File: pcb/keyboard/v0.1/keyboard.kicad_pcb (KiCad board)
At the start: 2 copper layers, 80.8 x 79.7 mm, 142 parts, among them J1 USB2.0, J2 SWD, SW1 BACKTICK, SW10 9, SW11 0, SW12 BACKSPACE, SW13 TAB, SW14 Q, SW15 W, SW16 E, SW17 R, SW18 T, SW19 Y, SW2 1, SW20 U, SW21 I, SW22 O, SW23 P, SW24 RETURN, SW25 CAPS, SW26 A, SW27 S, SW28 D, SW29 F, SW3 2, SW30 G, SW31 H, SW32 J, SW33 K, SW34 L, SW35 SEMI, SW36 QUOTE, SW37 LSHIFT, SW38 Z, SW39 X, SW4 3, SW40 C, SW41 V, SW42 B, SW43 N, SW44 M, SW45 COMMA, SW46 DOT, SW47 QUEST, SW48 RSHIFT, SW49 FN, SW5 4, SW50 LCTRL, SW51 LSUPER, SW52 LALT, SW53 SPACE, SW54 RALT, SW55 RSUPER, SW56 MENU, SW57 RCTRL, SW58 C1, SW59 C2, SW6 5, SW60 C3, SW61 C4, SW62 C5, SW63 C6, SW7 6, SW8 7, SW9 8, U1 MDBT50Q-P1MV2, Y1 32.768

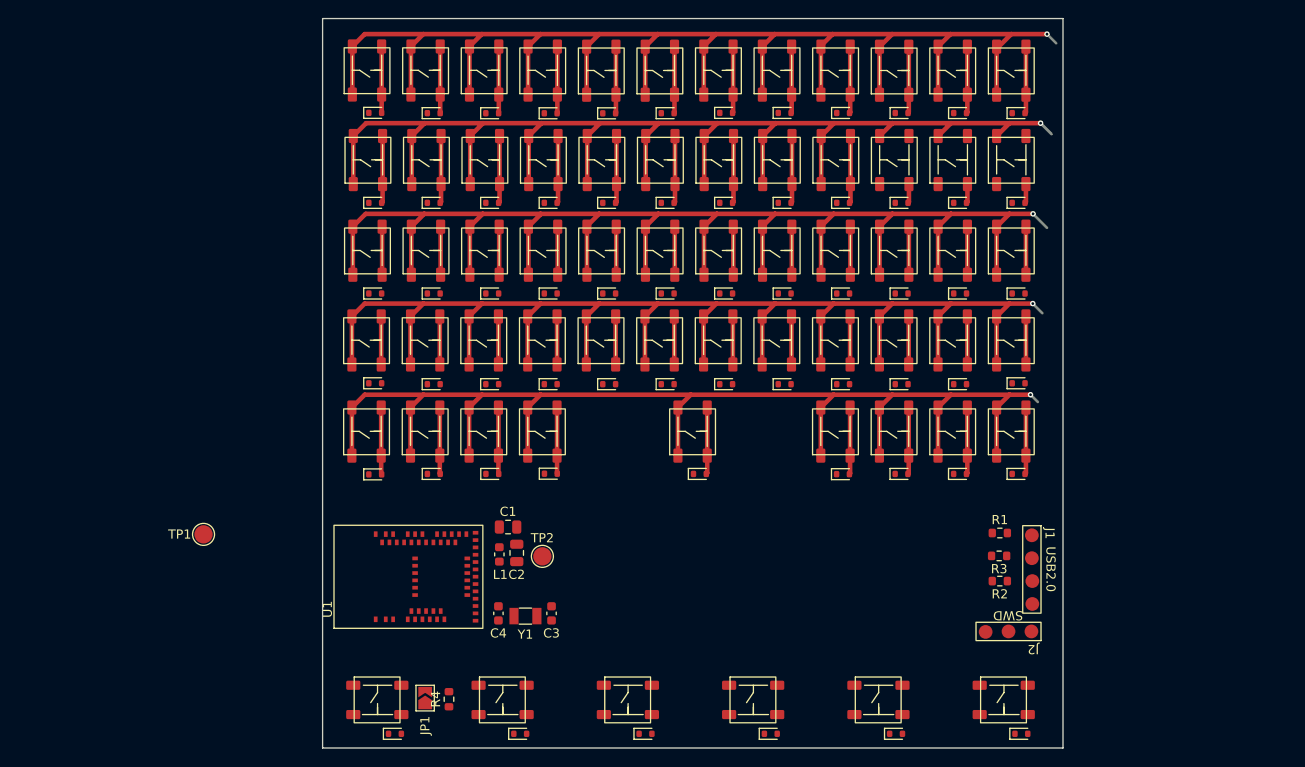
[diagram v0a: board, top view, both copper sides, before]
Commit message: Add RF keepout zone for main chip
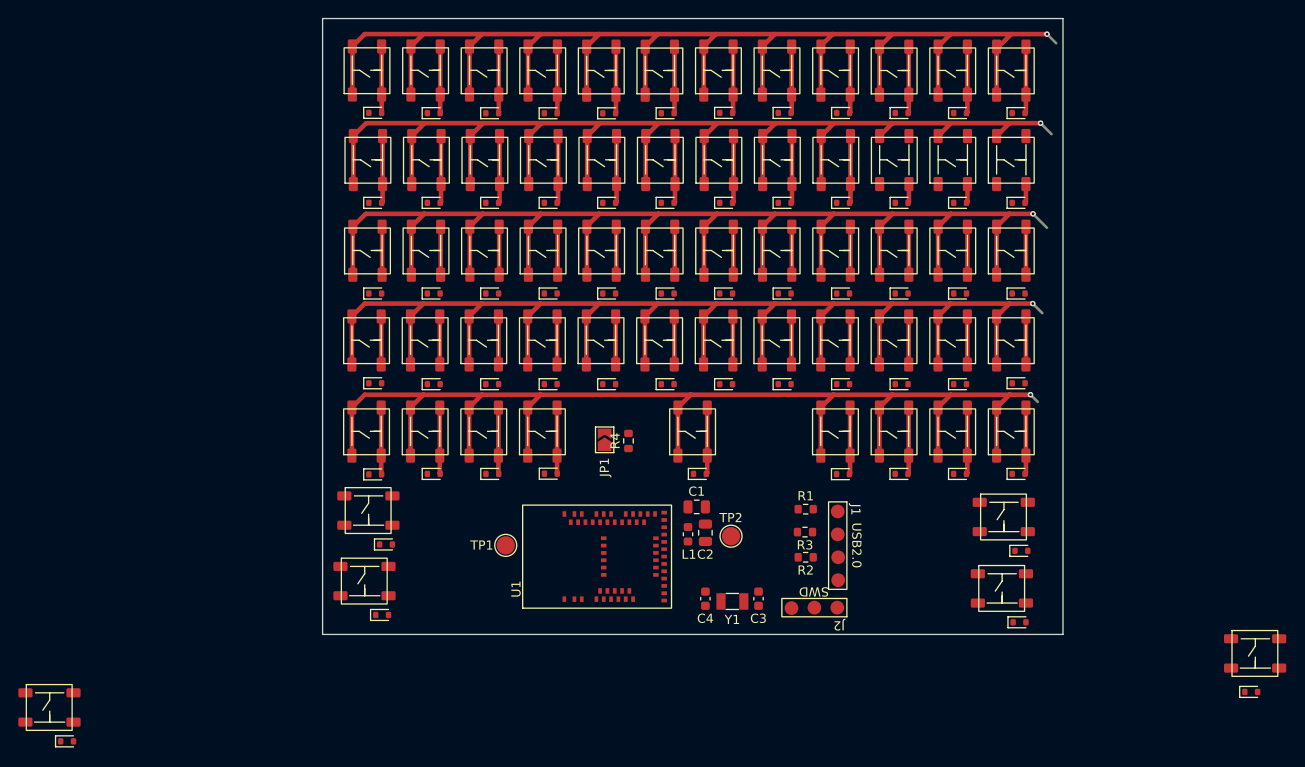
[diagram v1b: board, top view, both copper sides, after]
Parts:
- moved D60 63.2 mm to (28.5, 112.2)
- moved SW60 63.2 mm to (23.9, 106.9)
- moved JP1 34.3 mm to (87.2, 79.3)
- moved R4 34.3 mm to (89.8, 79.4)
- moved SW61 33.9 mm to (128.2, 86.1)
- moved D61 33.9 mm to (132.7, 91.4)
- moved TP1 33.0 mm to (76.4, 90.8)
- moved SW63 27.9 mm to (155.6, 101.0)
- moved D63 25.5 mm to (157.8, 106.8)
- moved Y1 22.7 mm to (101.2, 96.9)
- moved C4 22.7 mm to (98.2, 96.6)
- moved C3 22.7 mm to (104.0, 96.6)
- moved J2 21.4 mm to (112.6, 97.6)
- moved R3 21.4 mm to (109.1, 89.3)
- moved J1 21.4 mm to (112.7, 87.1)
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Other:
- board size 80.8 x 79.7 mm -> 80.8 x 67.2 mm
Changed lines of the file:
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@@
 	(footprint "TH-A1OC:tact_switch_4.5x4.5_PTS647"
 		(layer "F.Cu")
-		(at 73.43 106.075)
+		(at 58.35 93.1)
 		(property "Reference" "SW59"
 			(at 1 5 0)
@@
 	(footprint "TH-A1OC:tact_switch_4.5x4.5_PTS647"
 		(layer "F.Cu")
-		(at 59.75 106.075)
+		(at 58.775 85.4)
 		(property "Reference" "SW58"
 			(at 1 5 0)
@@
 	(footprint "Resistor_SMD:R_0603_1608Metric"
 		(layer "F.Cu")
-		(at 130.275 91.95 180)
+		(at 109.075 89.35 180)
 		(descr "Resistor SMD 0603 (1608 Metric), square (rectangular) end terminal, IPC-7351 nominal, (Body size source: IPC-SM-782 page 72, https://www.pcb-3d.com/wordpress/wp-content/uploads/ipc-sm-782a_amendment_1_and_2.pdf), generated with kicad-footprint-generator")
 		(tags "resistor")
@@
 	(footprint "TH-A1OC:th_pogo_pins_4"
 		(layer "F.Cu")
-		(at 133.85 89.7 -90)
+		(at 112.65 87.1 -90)
 		(property "Reference" "J1"
 			(at -0.2 -1.95 270)
@@
 	(footprint "Diode_SMD:D_SOD-523"
 		(layer "F.Cu")
-		(at 77.98 111.375)
+		(at 62.9 98.4)
 		(descr "http://www.diodes.com/datasheets/ap02001.pdf p.144")
 		(tags "Diode SOD523")
@@
 	(footprint "Capacitor_SMD:C_0805_2012Metric"
 		(layer "F.Cu")
-		(at 77.6 91.625 90)
+		(at 98.2 89.425 90)
 		(descr "Capacitor SMD 0805 (2012 Metric), square (rectangular) end terminal, IPC-7351 nominal, (Body size source: IPC-SM-782 page 76, https://www.pcb-3d.com/wordpress/wp-content/uploads/ipc-sm-782a_amendment_1_and_2.pdf, https://docs.google.com/spreadsheets/d/1BsfQQcO9C6DZCsRaXUlFlo91Tg2WpOkGARC1WS5S8t0/edit?usp=sharing), generated with kicad-footprint-generator")
 		(tags "capacitor")
@@
 	(footprint "TestPoint:TestPoint_Pad_D2.0mm"
 		(layer "F.Cu")
-		(at 43.4 89.6)
+		(at 76.4 90.8)
 		(descr "SMD pad as test Point, diameter 2.0mm")
 		(tags "test point SMD pad")
@@
 	(footprint "TH-A1OC:tact_switch_4.5x4.5_PTS647"
 		(layer "F.Cu")
-		(at 100.79 106.075)
+		(at 128.15 86.1)
 		(property "Reference" "SW61"
 			(at 1 5 0)
@@
 	(footprint "Capacitor_SMD:C_0603_1608Metric"
 		(layer "F.Cu")
-		(at 75.6 98.225 90)
+		(at 98.2 96.625 90)
 		(descr "Capacitor SMD 0603 (1608 Metric), square (rectangular) end terminal, IPC-7351 nominal, (Body size source: IPC-SM-782 page 76, https://www.pcb-3d.com/wordpress/wp-content/uploads/ipc-sm-782a_amendment_1_and_2.pdf), generated with kicad-footprint-generator")
 		(tags "capacitor")
@@
 	(footprint "Diode_SMD:D_SOD-523"
 		(layer "F.Cu")
-		(at 132.7 111.375)
+		(at 157.8 106.8)
 		(descr "http://www.diodes.com/datasheets/ap02001.pdf p.144")
 		(tags "Diode SOD523")
@@
 	(footprint "TH-A1OC:tact_switch_4.5x4.5_PTS647"
 		(layer "F.Cu")
-		(at 128.15 106.075)
+		(at 155.6 101)
 		(property "Reference" "SW63"
 			(at 1 5 0)
@@
 	(footprint "TestPoint:TestPoint_Pad_D2.0mm"
 		(layer "F.Cu")
-		(at 80.4 92)
+		(at 101 89.8)
 		(descr "SMD pad as test Point, diameter 2.0mm")
 		(tags "test point SMD pad")
@@
 	(footprint "Diode_SMD:D_SOD-523"
 		(layer "F.Cu")
-		(at 119.02 111.375)
+		(at 132.5 99.2)
 		(descr "http://www.diodes.com/datasheets/ap02001.pdf p.144")
 		(tags "Diode SOD523")
@@
 	(footprint "Diode_SMD:D_SOD-523"
 		(layer "F.Cu")
-		(at 105.34 111.375)
+		(at 132.7 91.4)
 		(descr "http://www.diodes.com/datasheets/ap02001.pdf p.144")
 		(tags "Diode SOD523")
@@
 	(footprint "Capacitor_SMD:C_0805_2012Metric"
 		(layer "F.Cu")
-		(at 76.65 88.8)
+		(at 97.25 86.6)
 		(descr "Capacitor SMD 0805 (2012 Metric), square (rectangular) end terminal, IPC-7351 nominal, (Body size source: IPC-SM-782 page 76, https://www.pcb-3d.com/wordpress/wp-content/uploads/ipc-sm-782a_amendment_1_and_2.pdf, https://docs.google.com/spreadsheets/d/1BsfQQcO9C6DZCsRaXUlFlo91Tg2WpOkGARC1WS5S8t0/edit?usp=sharing), generated with kicad-footprint-generator")
 		(tags "capacitor")
@@
 	(footprint "Resistor_SMD:R_0603_1608Metric"
 		(layer "F.Cu")
-		(at 70.2 107.6 90)
+		(at 89.8 79.4 90)
 		(descr "Resistor SMD 0603 (1608 Metric), square (rectangular) end terminal, IPC-7351 nominal, (Body size source: IPC-SM-782 page 72, https://www.pcb-3d.com/wordpress/wp-content/uploads/ipc-sm-782a_amendment_1_and_2.pdf), generated with kicad-footprint-generator")
 		(tags "resistor")
@@
 	(footprint "Resistor_SMD:R_0603_1608Metric"
 		(layer "F.Cu")
-		(at 130.35 94.7 180)
+		(at 109.15 92.1 180)
 		(descr "Resistor SMD 0603 (1608 Metric), square (rectangular) end terminal, IPC-7351 nominal, (Body size source: IPC-SM-782 page 72, https://www.pcb-3d.com/wordpress/wp-content/uploads/ipc-sm-782a_amendment_1_and_2.pdf), generated with kicad-footprint-generator")
 		(tags "resistor")
@@
 	(footprint "TH-A1OC:tact_switch_4.5x4.5_PTS647"
 		(layer "F.Cu")
-		(at 87.11 106.075)
+		(at 23.95 106.9)
 		(property "Reference" "SW60"
 			(at 1 5 0)
@@
 	(footprint "Resistor_SMD:R_0603_1608Metric"
 		(layer "F.Cu")
-		(at 130.35 89.45)
+		(at 109.15 86.85)
 		(descr "Resistor SMD 0603 (1608 Metric), square (rectangular) end terminal, IPC-7351 nominal, (Body size source: IPC-SM-782 page 72, https://www.pcb-3d.com/wordpress/wp-content/uploads/ipc-sm-782a_amendment_1_and_2.pdf), generated with kicad-footprint-generator")
 		(tags "resistor")
@@
 	(footprint "Capacitor_SMD:C_0603_1608Metric"
 		(layer "F.Cu")
-		(at 81.4 98.225 90)
+		(at 104 96.625 90)
 		(descr "Capacitor SMD 0603 (1608 Metric), square (rectangular) end terminal, IPC-7351 nominal, (Body size source: IPC-SM-782 page 76, https://www.pcb-3d.com/wordpress/wp-content/uploads/ipc-sm-782a_amendment_1_and_2.pdf), generated with kicad-footprint-generator")
 		(tags "capacitor")
@@
 	(footprint "Diode_SMD:D_SOD-523"
 		(layer "F.Cu")
-		(at 64.3 111.375)
+		(at 63.325 90.7)
 		(descr "http://www.diodes.com/datasheets/ap02001.pdf p.144")
 		(tags "Diode SOD523")
@@
 	(footprint "TH-A1OC:th_pogo_pins_3"
 		(layer "F.Cu")
-		(at 133.8 100.2 180)
+		(at 112.6 97.6 180)
 		(property "Reference" "J2"
 			(at -0.2 -1.95 180)
@@
 	(footprint "Diode_SMD:D_SOD-523"
 		(layer "F.Cu")
-		(at 91.66 111.375)
+		(at 28.5 112.2)
 		(descr "http://www.diodes.com/datasheets/ap02001.pdf p.144")
 		(tags "Diode SOD523")
@@
 	(footprint "TH-A1OC:tact_switch_4.5x4.5_PTS647"
 		(layer "F.Cu")
-		(at 114.47 106.075)
+		(at 127.95 93.9)
 		(property "Reference" "SW62"
 			(at 1 5 0)
@@
 	(footprint "TH-A1OC:TH_MDBT50Q-P1MV2"
 		(layer "F.Cu")
-		(at 57.6 99.974998 90)
+		(at 78.2 97.774998 90)
 		(property "Reference" "U1"
 			(at 2.1951 -0.653001 90)
@@
 			(layer "F.Fab")
 		)
+		(fp_rect
+			(start -3.275 -2.1)
+			(end 14.775 4.3)
+			(stroke
+				(width 0.05)
+				(type solid)
+			)
+			(fill no)
+			(layer "F.Fab")
+		)
 		(fp_text user "${REFERENCE}"
 			(at 5.7442 8.195999 90)
@@
 			(pintype "bidirectional+no_connect")
 		)
+		(zone
+			(net 0)
+			(net_name "")
+			(layers "F.Cu" "B.Cu" "F.CrtYd")
+			(name "RF keepout zone")
+			(hatch edge 0.5)
+			(connect_pads
+				(clearance 0)
+			)
+			(min_thickness 0.25)
+			(filled_areas_thickness no)
+			(keepout
+				(tracks not_allowed)
+				(vias not_allowed)
+				(pads allowed)
+				(copperpour not_allowed)
+				(footprints allowed)
+			)
+			(placement
+				(enabled no)
+				(sheetname "")
+			)
+			(fill
+				(thermal_gap 0.5)
+				(thermal_bridge_width 0.5)
+			)
+			(polygon
+				(pts
+					(xy 76.15 101.024998) (xy 76.15 83.024998) (xy 82.5 83.024998) (xy 82.5 101.024998)
+				)
+			)
+		)
 		(embedded_fonts no)
 	)
@@
 	(footprint "Jumper:SolderJumper-2_P1.3mm_Open_TrianglePad1.0x1.5mm"
 		(layer "F.Cu")
-		(at 67.6 107.475 90)
+		(at 87.2 79.275 90)
 		(descr "SMD Solder Jumper, 1x1.5mm Triangular Pads, 0.3mm gap, open")
 		(tags "solder jumper open")
@@
 	(footprint "Inductor_SMD:L_0603_1608Metric"
 		(layer "F.Cu")
-		(at 75.7 91.7875 -90)
+		(at 96.3 89.5875 -90)
 		(descr "Inductor SMD 0603 (1608 Metric), square (rectangular) end terminal, IPC-7351 nominal, (Body size source: http://www.tortai-tech.com/upload/download/2011102023233369053.pdf), generated with kicad-footprint-generator")
 		(tags "inductor")
@@
 	(footprint "Crystal:Crystal_SMD_3215-2Pin_3.2x1.5mm"
 		(layer "F.Cu")
-		(at 78.55 98.525 180)
+		(at 101.15 96.925 180)
 		(descr "SMD Crystal FC-135 https://support.epson.biz/td/api/doc_check.php?dl=brief_FC-135R_en.pdf")
 		(tags "SMD SMT Crystal")
@@
 	(gr_rect
 		(start 56.4 33.275)
-		(end 137.25 112.925)
+		(end 137.25 100.525)
 		(stroke
 			(width 0.05)

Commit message: 2 layers was never going to be enough
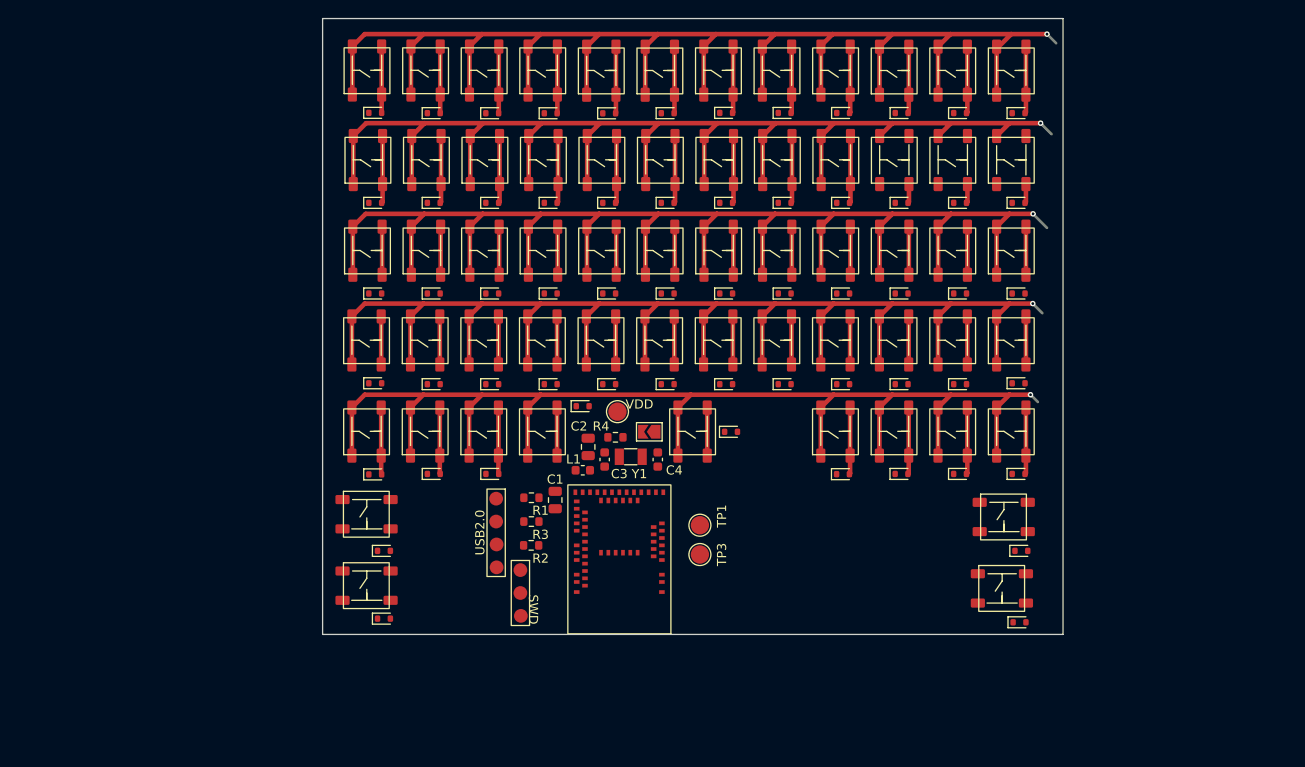
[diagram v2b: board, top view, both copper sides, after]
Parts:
- removed D58, D63: 1N4148, Diode_SMD:D_SOD-523
- removed SW58: C1, TH-A1OC:tact_switch_4.5x4.5_PTS647
- removed SW63: C6, TH-A1OC:tact_switch_4.5x4.5_PTS647
- added TP3: TestPoint, TestPoint:TestPoint_Pad_D2.0mm, F.Cu at (97.6, 91.8)
- moved J1 37.3 mm to (75.3, 85.7)
- moved D60 37.1 mm to (63.1, 98.8)
- moved SW60 37.1 mm to (58.6, 93.6)
- moved J2 34.8 mm to (78.0, 93.5), turned to -90 degrees
- moved R2 30.0 mm to (79.2, 90.8)
- moved R1 30.0 mm to (79.2, 85.6)
- moved R3 29.9 mm to (79.2, 88.2)
- moved C3 22.7 mm to (87.2, 81.4)
- moved TP1 21.3 mm to (97.6, 88.6)
- moved Y1 19.3 mm to (90.0, 81.1), turned to 0 degrees
- moved TP2 18.4 mm to (88.6, 76.2), turned to 90 degrees
- moved U1 16.6 mm to (94.6, 100.5), turned to 180 degrees
- moved C4 16.1 mm to (93.0, 81.4), turned to -90 degrees
- moved C2 15.9 mm to (85.4, 80.0)
- moved C1 15.5 mm to (81.8, 85.8), turned to -90 degrees
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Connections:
- net Net-(U1B-DCCH) renamed /DCCH
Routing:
- net Net-(D53-A): track 7.29 -> 5.25 mm
- net Net-(D52-A): track 7.24 -> 5.25 mm
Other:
- copper layers 2 -> 4
- board text added: "VDD"
